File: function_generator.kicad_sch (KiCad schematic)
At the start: 0 parts

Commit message: Added Symbols and Dual Boost Circuit
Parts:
- added C? (x2): ???, symbol Device:C_Small
- added C?: 10nF, symbol Device:C_Small
- added C?: 1uF, Capacitor_SMD:C_0805_2012Metric_Pad1.18x1.45mm_HandSolder, symbol Device:C
- added C?: 4.7nF, symbol Device:C_Small
- added C?: 220nF, symbol Device:C_Small
- added C?: 0.1uF, symbol Device:C_Small
- added C? (x2): ???uF, symbol Device:C_Small
- added C? (x2): 22uF, symbol Device:C_Small
- added C?: 1uF, symbol Device:C_Small
- added D? (x2): MBR120, Diode_SMD:D_SOD-123F, symbol Device:D_Schottky_Small
- added J1: USB C 2.0, Connector_USB:USB_C_Receptacle_G-Switch_GT-USB-7010ASV, symbol Connector:USB_C_Receptacle_USB2.0_14P
- added L? (x2): 4.7uH, symbol Device:L
- added Q?: AO3401A, Package_TO_SOT_SMD:SOT-23, symbol Transistor_FET:AO3401A
- added R23, R24: 5.1k, Resistor_SMD:R_0805_2012Metric_Pad1.20x1.40mm_HandSolder, symbol Device:R_Small_US
- added R? (x4): ???, symbol Device:R_Small_US
- added R?: 10k, Resistor_SMD:R_0805_2012Metric_Pad1.20x1.40mm_HandSolder, symbol Device:R_US
- added R?: 100, symbol Device:R_Small_US
- added SW?: Reset, Button_Switch_SMD:SW_SPST_CK_RS282G05A3, symbol Switch:SW_Push
- added U1: ATSAMD21E18A-M, Package_DFN_QFN:QFN-32-1EP_5x5mm_P0.5mm_EP3.6x3.6mm, symbol MCU_Microchip_SAMD:ATSAMD21E18A-M
- added U?: LT3045xMSE, Package_SO:MSOP-12-1EP_3x4.039mm_P0.65mm_EP1.651x2.845mm, symbol Regulator_Linear:LT3045xMSE
- added U?: LT3094xMSE, Package_SO:MSOP-12-1EP_3x4.039mm_P0.65mm_EP1.651x2.845mm, symbol Regulator_Linear:LT3094xMSE
- added U?: TPS65131RGE, Package_DFN_QFN:VQFN-24-1EP_4x4mm_P0.5mm_EP2.45x2.45mm_ThermalVias, symbol Regulator_Switching:TPS65131RGE
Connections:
- new net: C?.1, L?.1, Q?.3 (D)
- new net: D?.2 (A), L?.2, U?.1 (INP), U?.24 (INP)
- new net: C?.2, R?.1, R?.2, U?.22 (FBP)
- new net: C?.1, U?.21 (CP)
- new net: U?.1 (IN), U?.2 (IN), U?.3 (IN)
- new net: U?.11 (OUT), U?.12 (OUT) (x2)
- new net: U?.13 (GND), U?.9 (GND)
- new net: C?.1, U1.29 (VDDCORE)
- new net: U?.1 (IN), U?.13 (IN), U?.2 (IN)
- new net: C?.1, U?.18 (CN)
- new net: D?.1 (K), L?.1, U?.13 (OUTN), U?.14 (OUTN)
- new net: C?.1, R?.1, R?.2, U?.16 (FBN)
- new net: C?.1, R?.2, U?.17 (VREF)
- new net: C?.1, R?.2, U?.4 (VIN)
- new net: Q?.1 (G), U?.7 (BSW)
- new net +3.3V: U1.30 (VDDIN), U1.9 (VDDANA)
- new net +3V3: R?.2
- new net CC1: J1.A5 (CC1), R24.2
- new net CC2: J1.B5 (CC2), R23.2
- new net D+: J1.A6 (D+), J1.B6 (D+)
- new net D-: J1.A7 (D-), J1.B7 (D-)
- new net GND: C?.2, C?.2, C?.2, C?.2, C?.2, C?.2, C?.2, C?.2, C?.2, C?.2, J1.A1 (GND), J1.A12 (GND), J1.B1 (GND), J1.B12 (GND), J1.S1 (SHIELD), L?.2, R23.1, R24.1, R?.1, SW?.2, U1.10 (GND), U1.28 (GND), U1.33 (EP), U?.19 (GND), U?.2 (GND), U?.25 (EP), U?.3 (PGND)
- new net RST: C?.1, R?.1, SW?.1, U1.26 (~{RESET})
- new net VBus: C?.1, J1.A4 (VBUS), J1.A9 (VBUS), J1.B4 (VBUS), J1.B9 (VBUS), Q?.2 (S), R?.1, U?.5 (INN), U?.6 (INN)
- new net VNeg: C?.1, C?.2, D?.2 (A), R?.1, U?.15 (VNEG)
- new net VPos: C?.1, C?.1, D?.1 (K), R?.2, U?.23 (VPOS)
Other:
- note added: "MCU Reset"
- note added: "TPS65131 Dual Boost Supply"
- note added: "USB C 2.0 Interface"

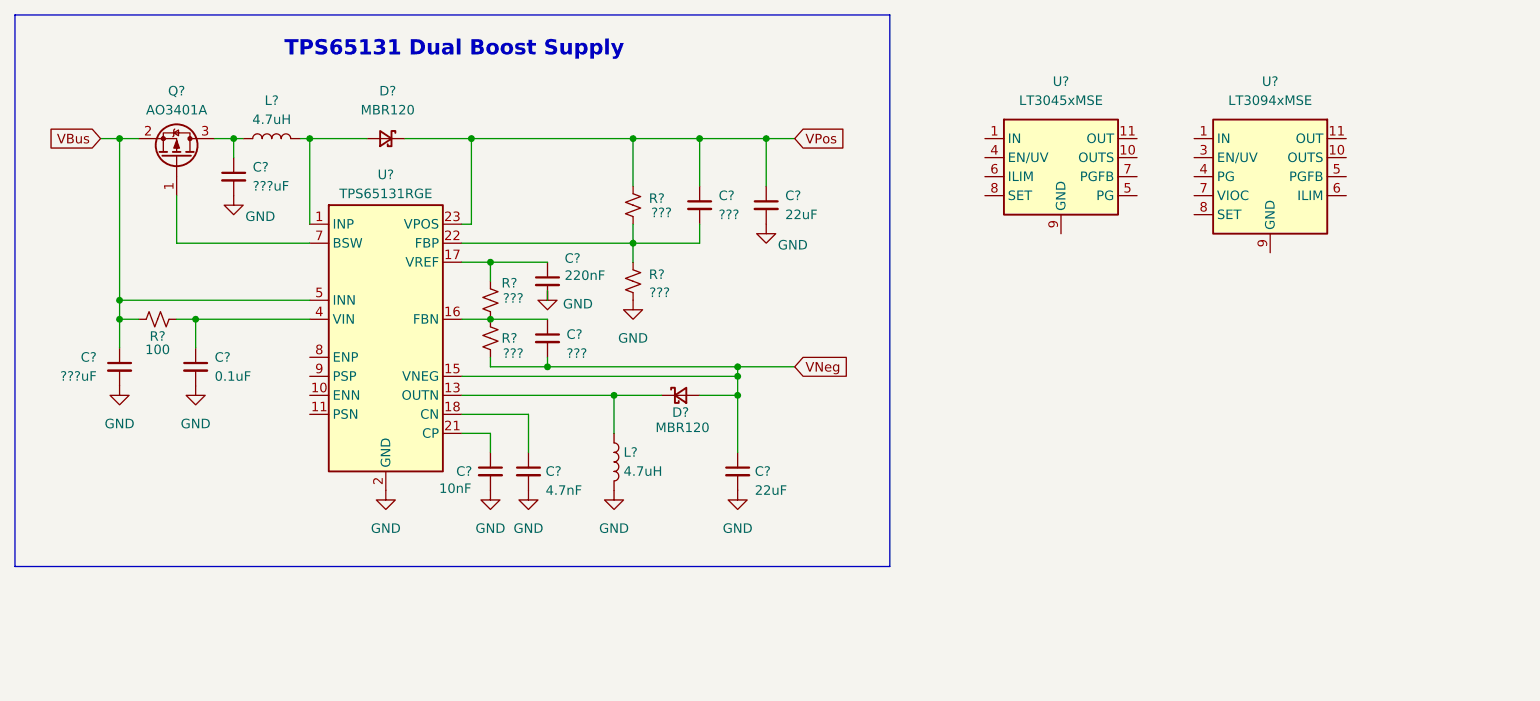
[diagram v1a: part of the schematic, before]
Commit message: Boost converter circuit calculations
Organized schematic by placing boost converter in a sub-sheet. Calculated resistor values for boost converter feedback, setting outputs to approximately +/- 12.77V.
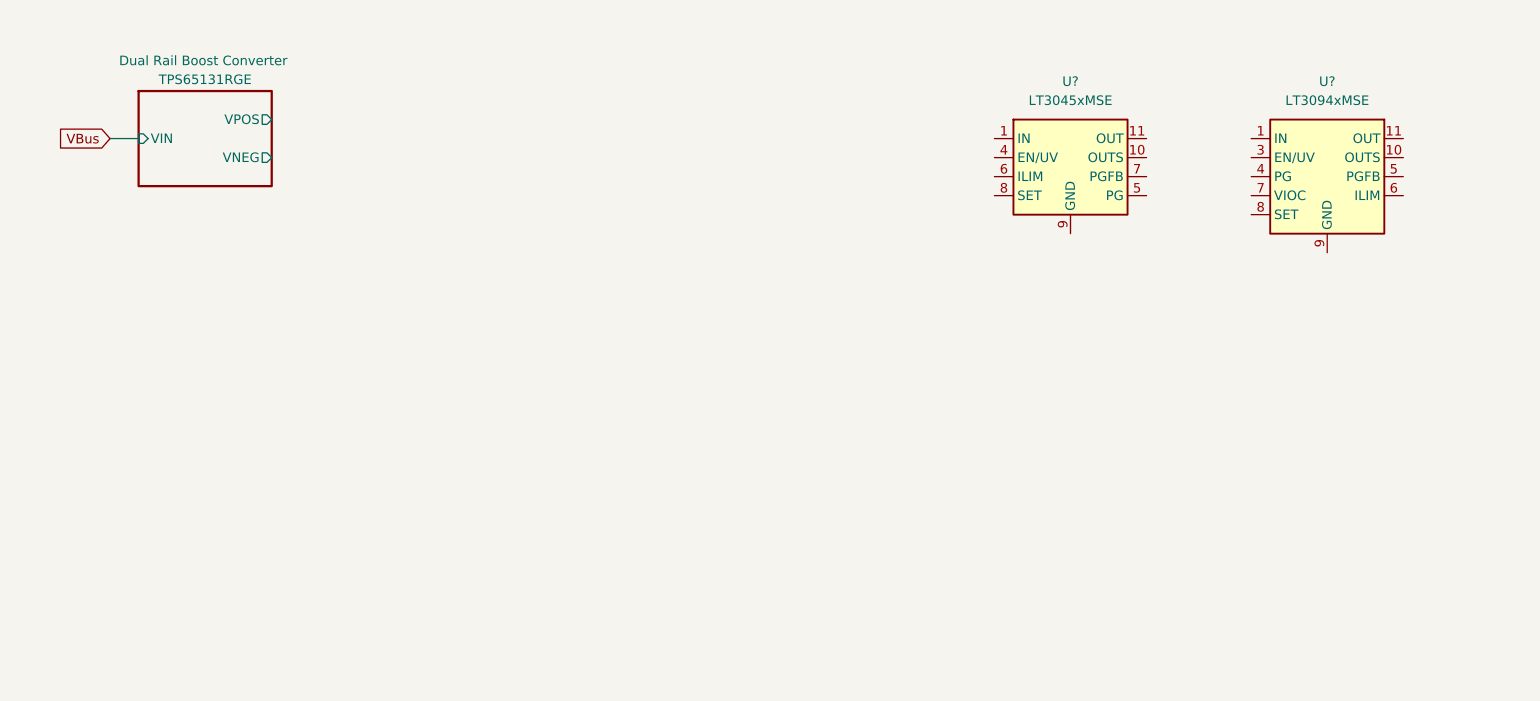
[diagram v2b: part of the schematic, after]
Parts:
- removed C? (x2): ???, symbol Device:C_Small
- removed C?: 10nF, symbol Device:C_Small
- removed C?: 4.7nF, symbol Device:C_Small
- removed C?: 220nF, symbol Device:C_Small
- removed C?: 0.1uF, symbol Device:C_Small
- removed C? (x2): ???uF, symbol Device:C_Small
- removed C? (x2): 22uF, symbol Device:C_Small
- removed D? (x2): MBR120, Diode_SMD:D_SOD-123F, symbol Device:D_Schottky_Small
- removed L? (x2): 4.7uH, symbol Device:L
- removed Q?: AO3401A, Package_TO_SOT_SMD:SOT-23, symbol Transistor_FET:AO3401A
- removed R? (x4): ???, symbol Device:R_Small_US
- removed R?: 100, symbol Device:R_Small_US
- removed U?: TPS65131RGE, Package_DFN_QFN:VQFN-24-1EP_4x4mm_P0.5mm_EP2.45x2.45mm_ThermalVias, symbol Regulator_Switching:TPS65131RGE
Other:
- added sheet Dual Rail Boost Converter (boost_coverter.kicad_sch)
- note removed: "TPS65131 Dual Boost Supply"
- moved on the sheet: U?

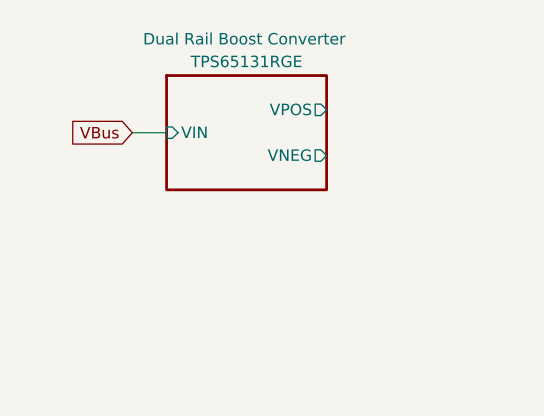
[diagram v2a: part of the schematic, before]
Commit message: Finished TPS65131 schematic.
Finalized inductor and capacitor calculations. Exposed EN pin with pull-downs for default off state. Disabled low-power/burst mode.
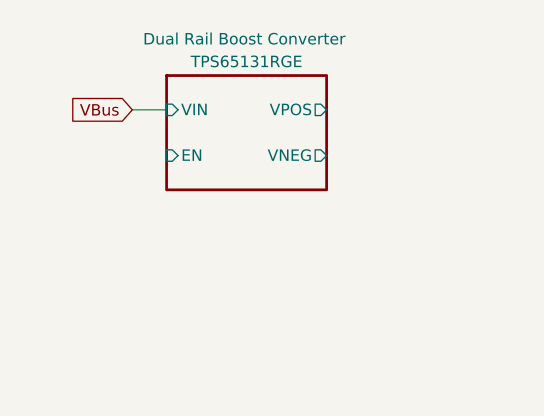
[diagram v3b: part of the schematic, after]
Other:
- sheet Dual Rail Boost Converter ports: added EN; removed none
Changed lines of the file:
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@@
 	(wire
 		(pts
-			(xy 26.67 30.48) (xy 30.48 30.48)
+			(xy 26.67 27.94) (xy 30.48 27.94)
 		)
 		(stroke
@@
 	(global_label "VBus"
 		(shape input)
-		(at 26.67 30.48 180)
+		(at 26.67 27.94 180)
 		(fields_autoplaced yes)
 		(effects
@@
 		)
 		(property "Intersheetrefs" "${INTERSHEET_REFS}"
-			(at 19.1491 30.48 0)
+			(at 19.1491 27.94 0)
 			(effects
 				(font
@@
 		)
 		(pin "VIN" input
-			(at 30.48 30.48 180)
+			(at 30.48 27.94 180)
 			(effects
 				(font
@@
 			)
 		)
+		(pin "EN" input
+			(at 30.48 33.02 180)
+			(effects
+				(font
+					(size 1.27 1.27)
+				)
+				(justify left)
+			)
+		)
